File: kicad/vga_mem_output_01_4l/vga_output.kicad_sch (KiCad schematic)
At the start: 16 parts, among them J1 Conn_01x03_Socket, J4 DE15_Socket_HighDensity_Mount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, U1 74LS08, U2 74LS08

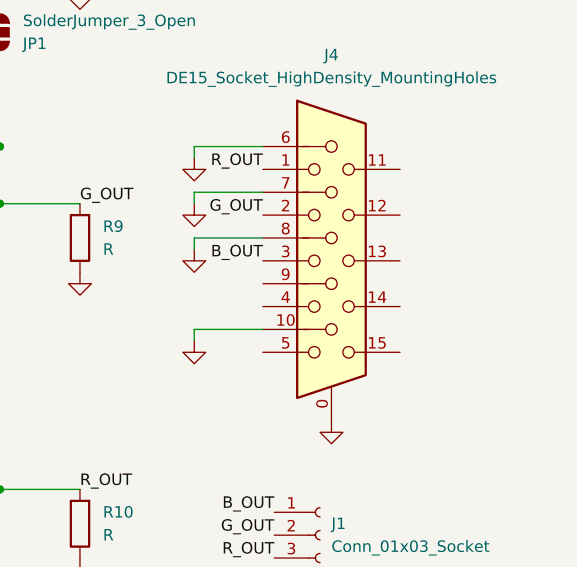
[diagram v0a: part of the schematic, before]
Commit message: added clock circuit ('display generator')
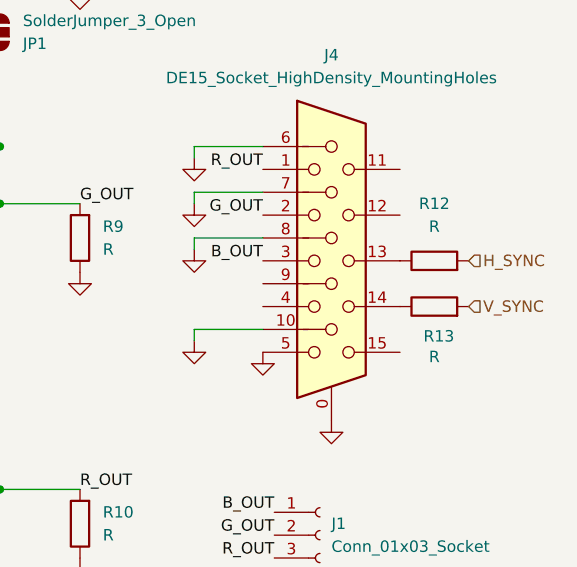
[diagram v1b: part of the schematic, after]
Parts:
- added R12, R13: R, Resistor_THT:R_Axial_DIN0204_L3.6mm_D1.6mm_P7.62mm_Horizontal, symbol Device:R
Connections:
- net GND: now also J4.5
- net at J4.13: now also R12.1
- net at J4.14: now also R13.1
- new net H_SYNC: R12.2
- new net V_SYNC: R13.2
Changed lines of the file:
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@@
+		)
+	)
+	(hierarchical_label "H_SYNC"
+		(shape input)
+		(at 143.51 95.25 0)
+		(effects
+			(font
+				(size 1.27 1.27)
+			)
+			(justify left)
 		)
 	)
@@
 		)
 	)
+	(hierarchical_label "V_SYNC"
+		(shape input)
+		(at 143.51 100.33 0)
+		(effects
+			(font
+				(size 1.27 1.27)
+			)
+			(justify left)
+		)
+	)
 	(hierarchical_label "VA_EN"
 		(shape input)
@@
 	)
 	(symbol
+		(lib_id "Device:R")
+		(at 139.7 100.33 90)
+		(unit 1)
+		(exclude_from_sim no)
+		(in_bom yes)
+		(on_board yes)
+		(dnp no)
+		(property "Reference" "R13"
+			(at 140.208 103.632 90)
+			(effects
+				(font
+					(size 1.27 1.27)
+				)
+			)
+		)
+		(property "Value" "R"
+			(at 139.7 105.918 90)
+			(effects
+				(font
+					(size 1.27 1.27)
+				)
+			)
+		)
+		(property "Footprint" "Resistor_THT:R_Axial_DIN0204_L3.6mm_D1.6mm_P7.62mm_Horizontal"
+			(at 139.7 102.108 90)
+			(effects
+				(font
+					(size 1.27 1.27)
+				)
+				(hide yes)
+			)
+		)
+		(property "Datasheet" "~"
+			(at 139.7 100.33 0)
+			(effects
+				(font
+					(size 1.27 1.27)
+				)
+				(hide yes)
+			)
+		)
+		(property "Description" "Resistor"
+			(at 139.7 100.33 0)
+			(effects
+				(font
+					(size 1.27 1.27)
+				)
+				(hide yes)
+			)
+		)
+		(pin "2"
+		)
+		(pin "1"
+		)
+		(instances
+			(project "vga_mem_output_01_4l"
+				(path "/cb13e431-64f0-4016-a936-ee98aca3391f/f3e73905-7851-4c7b-a7de-c0801b7173ba"
+					(reference "R13")
+					(unit 1)
+				)
+			)
+		)
+	)
+	(symbol
 		(lib_id "power:GND")
 		(at 113.03 88.9 0)
@@
 	)
 	(symbol
+		(lib_id "Device:R")
+		(at 139.7 95.25 90)
+		(unit 1)
+		(exclude_from_sim no)
+		(in_bom yes)
+		(on_board yes)
+		(dnp no)
+		(fields_autoplaced yes)
+		(property "Reference" "R12"
+			(at 139.7 88.9 90)
+			(effects
+				(font
+					(size 1.27 1.27)
+				)
+			)
+		)
+		(property "Value" "R"
+			(at 139.7 91.44 90)
+			(effects
+				(font
+					(size 1.27 1.27)
+				)
+			)
+		)
+		(property "Footprint" "Resistor_THT:R_Axial_DIN0204_L3.6mm_D1.6mm_P7.62mm_Horizontal"
+			(at 139.7 97.028 90)
+			(effects
+				(font
+					(size 1.27 1.27)
+				)
+				(hide yes)
+			)
+		)
+		(property "Datasheet" "~"
+			(at 139.7 95.25 0)
+			(effects
+				(font
+					(size 1.27 1.27)
+				)
+				(hide yes)
+			)
+		)
+		(property "Description" "Resistor"
+			(at 139.7 95.25 0)
+			(effects
+				(font
+					(size 1.27 1.27)
+				)
+				(hide yes)
+			)
+		)
+		(pin "2"
+		)
+		(pin "1"
+		)
+		(instances
+			(project "vga_mem_output_01_4l"
+				(path "/cb13e431-64f0-4016-a936-ee98aca3391f/f3e73905-7851-4c7b-a7de-c0801b7173ba"
+					(reference "R12")
+					(unit 1)
+				)
+			)
+		)
+	)
+	(symbol
 		(lib_id "74xx:74LS08")
 		(at 71.12 107.95 0)
@@
 				)
 			)
+		)
+	)
+	(symbol
+		(lib_id "power:GND")
+		(at 120.65 105.41 0)
+		(unit 1)
+		(exclude_from_sim no)
+		(in_bom yes)
+		(on_board yes)
+		(dnp no)
+		(fields_autoplaced yes)
+		(property "Reference" "#PWR059"
+			(at 120.65 111.76 0)
+			(effects
+				(font
+					(size 1.27 1.27)
+				)
+				(hide yes)
+			)
+		)
+		(property "Value" "GND"
+			(at 120.65 110.49 0)
+			(effects
+				(font
+					(size 1.27 1.27)
+				)
+				(hide yes)
+			)
+		)
+		(property "Footprint" ""
+			(at 120.65 105.41 0)
+			(effects
+				(font
+					(size 1.27 1.27)
+				)
+				(hide yes)
+			)
+		)
+		(property "Datasheet" ""
+			(at 120.65 105.41 0)
+			(effects
+				(font
+					(size 1.27 1.27)
+				)
+				(hide yes)
+			)
+		)
+		(property "Description" ""
+			(at 120.65 105.41 0)
+			(effects
+				(font
+					(size 1.27 1.27)
+				)
+			)
+		)
+		(pin "1"
+		)
+		(instances
+			(project "vga_mem_output_01_4l"
+				(path "/cb13e431-64f0-4016-a936-ee98aca3391f/f3e73905-7851-4c7b-a7de-c0801b7173ba"
+					(reference "#PWR059")
+					(unit 1)
+				)
+			)

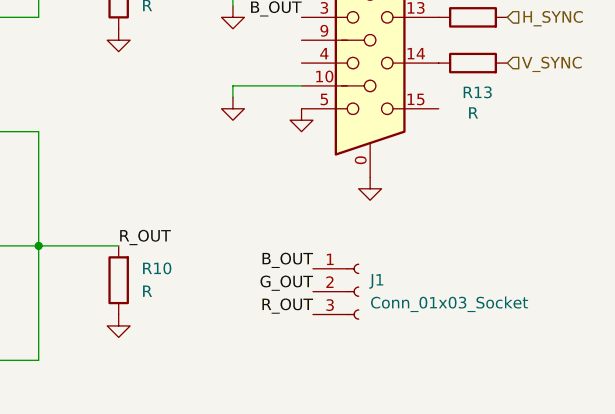
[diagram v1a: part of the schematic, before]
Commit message: finished vga rework
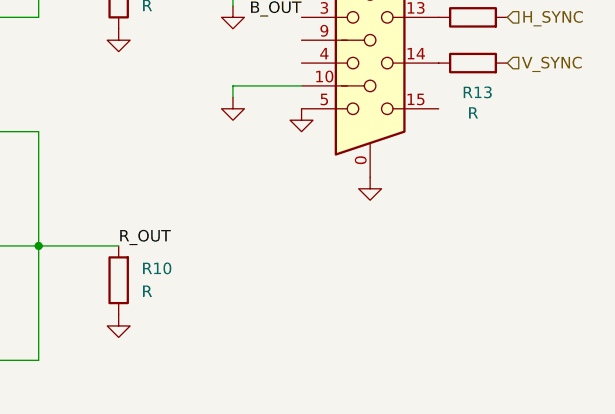
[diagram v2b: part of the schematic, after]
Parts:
- removed J1: Conn_01x03_Socket, Connector_PinSocket_2.54mm:PinSocket_1x03_P2.54mm_Vertical, symbol Connector:Conn_01x03_Socket
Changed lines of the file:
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@@
-		)
-	)
-	(label "G_OUT"
-		(at 121.92 125.73 180)
-		(effects
-			(font
-				(size 1.27 1.27)
-			)
-			(justify right bottom)
 		)
 	)
@@
 		)
 	)
-	(label "R_OUT"
-		(at 121.92 128.27 180)
-		(effects
-			(font
-				(size 1.27 1.27)
-			)
-			(justify right bottom)
-		)
-	)
 	(label "G_OUT"
 		(at 120.65 90.17 180)
@@
 	(label "B_OUT"
 		(at 120.65 95.25 180)
-		(effects
-			(font
-				(size 1.27 1.27)
-			)
-			(justify right bottom)
-		)
-	)
-	(label "B_OUT"
-		(at 121.92 123.19 180)
 		(effects
 			(font
@@
 					(unit 1)
 				)
-			)
-		)
-	)
-	(symbol
-		(lib_id "Connector:Conn_01x03_Socket")
-		(at 127 125.73 0)
-		(unit 1)
-		(exclude_from_sim no)
-		(in_bom yes)
-		(on_board yes)
-		(dnp no)
-		(fields_autoplaced yes)
-		(property "Reference" "J1"
-			(at 128.27 124.4599 0)
-			(effects
-				(font
-					(size 1.27 1.27)
-				)
-				(justify left)
-			)
-		)
-		(property "Value" "Conn_01x03_Socket"
-			(at 128.27 126.9999 0)
-			(effects
-				(font
-					(size 1.27 1.27)
-				)
-				(justify left)
-			)
-		)
-		(property "Footprint" "Connector_PinSocket_2.54mm:PinSocket_1x03_P2.54mm_Vertical"
-			(at 127 125.73 0)
-			(effects
-				(font
-					(size 1.27 1.27)
-				)
-				(hide yes)
-			)
-		)
-		(property "Datasheet" "~"
-			(at 127 125.73 0)
-			(effects
-				(font
-					(size 1.27 1.27)
-				)
-				(hide yes)
-			)
-		)
-		(property "Description" "Generic connector, single row, 01x03, script generated"
-			(at 127 125.73 0)
-			(effects
-				(font
-					(size 1.27 1.27)
-				)
-				(hide yes)
-			)
-		)
-		(pin "3"
-		)
-		(pin "1"
-		)
-		(pin "2"
-		)
-		(instances
-			(project "vga_mem_output_01_4l"
-				(path "/cb13e431-64f0-4016-a936-ee98aca3391f/f3e73905-7851-4c7b-a7de-c0801b7173ba"
-					(reference "J1")
-					(unit 1)
-				)
